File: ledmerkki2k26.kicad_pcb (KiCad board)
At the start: 2 copper layers, 52.2 x 74.7 mm, 71 parts, among them J1 Conn_01x03_Socket, J2 Conn_01x02_Pin, J3 Conn_01x06_Pin, SW1 SW_Push, U1 ATmega328PB-A, Y1 Resonator

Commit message: minor changes to pcb
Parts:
- moved C13 4.75 mm to (101.0, 97.6), turned to 0 degrees
- moved C7 1.28 mm to (90.3, 98.0)
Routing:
- net +5V: track 381.2 -> 379.0 mm
- net DATA: track 21.6 -> 22.6 mm

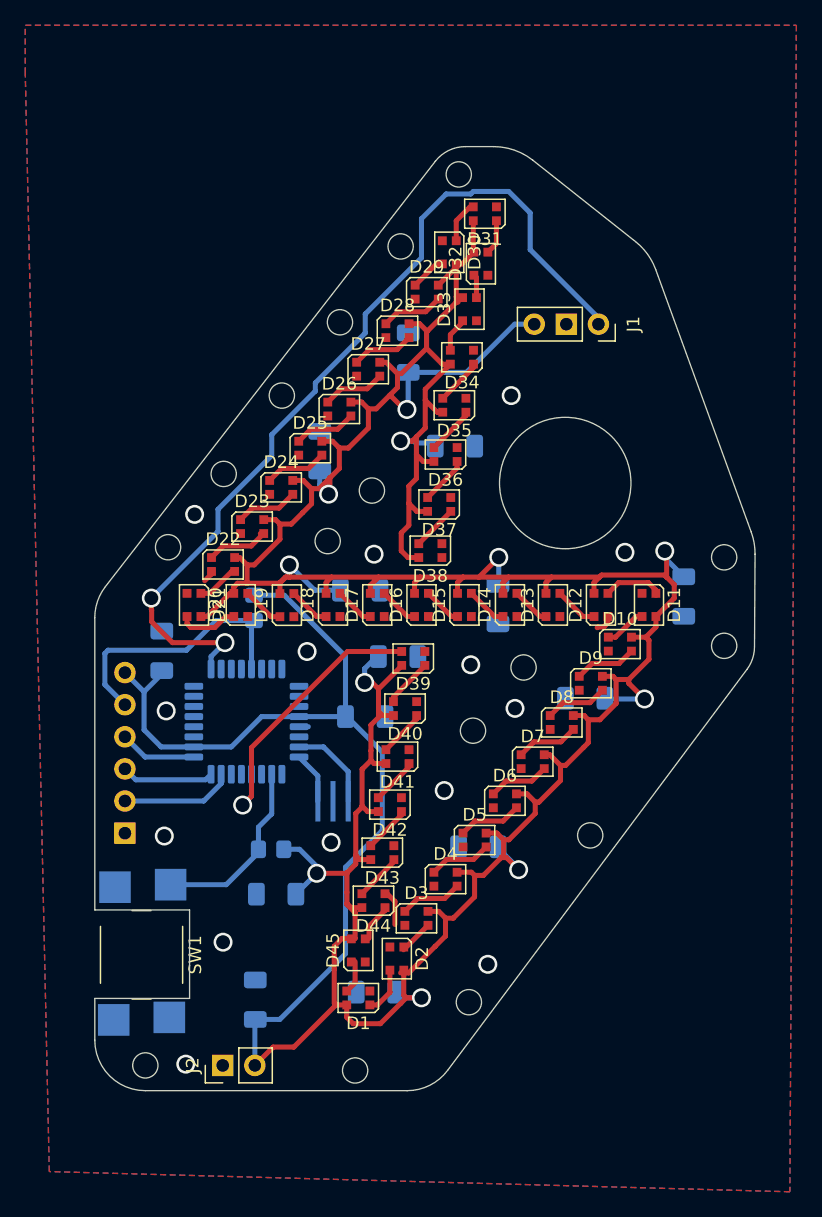
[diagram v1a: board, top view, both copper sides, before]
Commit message: updates to pcb layout and shape, uart pins exposed
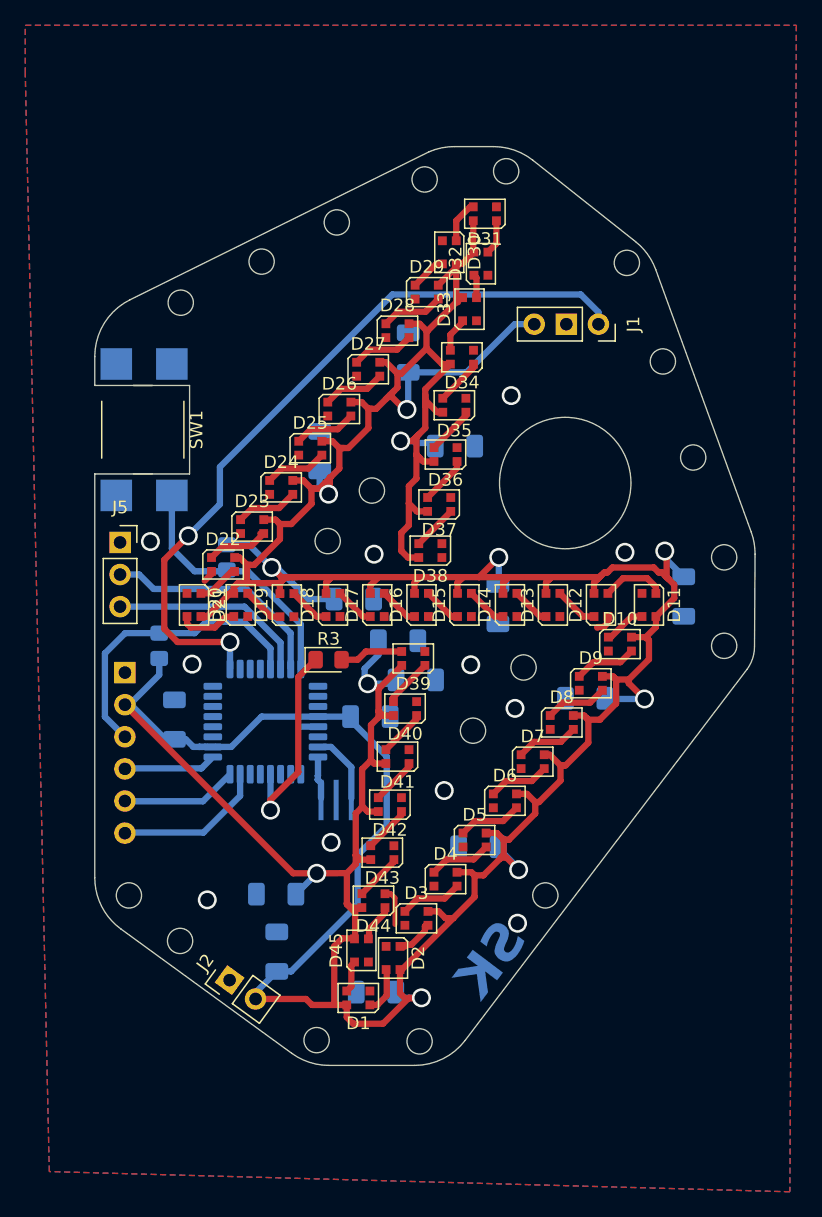
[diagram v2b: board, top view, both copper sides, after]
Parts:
- added C14: 500uF, Capacitor_SMD:C_1206_3216Metric_Pad1.33x1.80mm_HandSolder, B.Cu at (97.9, 116.1)
- added J5: uart, Connector_PinSocket_2.54mm:PinSocket_1x03_P2.54mm_Vertical, F.Cu at (74.5, 105.2)
- added R3: 500R, LED_SMD:LED_0805_2012Metric_Pad1.15x1.40mm_HandSolder, F.Cu at (91.0, 114.5)
- J1: value Conn_01x03_Socket -> mic module header
- J2: value Conn_01x02_Pin -> power header
- J3: value Conn_01x06_Pin -> ISP header
- moved ? 51.7 mm to (78.6, 91.1)
- moved SW1 41.6 mm to (78.6, 93.0)
- moved ? 41.5 mm to (74.2, 101.5)
- moved ? 41.4 mm to (74.2, 91.1)
- moved REF** 30.8 mm to (78.6, 101.5)
- moved R1 23.4 mm to (83.0, 106.4), turned to -90 degrees
- moved R2 8.08 mm to (77.6, 113.4), turned to 90 degrees
- moved J2 6.77 mm to (83.2, 139.8), turned to 54 degrees
- moved C12 5.53 mm to (78.8, 119.2)
- moved C1 4.16 mm to (86.9, 137.6)
- moved U1 1.50 mm to (86.0, 119.4)
- moved C9 1.25 mm to (96.5, 113.0)
- moved C4 0.86 mm to (93.0, 109.7)
- moved C2 0.40 mm to (94.3, 119.0)
- moved D2 0.30 mm to (96.1, 138.1)
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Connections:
- D39 pad 3: DATA -> Net-(D39-DIN)
- J3 pad 1: +5V -> GND
- J3 pad 2: /reset -> +5V
- J3 pad 3: /SCK -> /reset
- J3 pad 4: /MISO -> /SCK
- J3 pad 5: /MOSI -> /MISO
- J3 pad 6: GND -> /MOSI
- U1 pad 10: /button -> unconnected-(U1-PD6-Pad10)
- U1 pad 32: unconnected-(U1-PD2-Pad32) -> /button
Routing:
- net /UART_TX: track 0.00 -> 18.3 mm
- net /UART_RX: track 0.00 -> 16.0 mm
- net /dac: track 71.0 -> 59.6 mm
- net +5V: track 379.0 -> 387.8 mm
- net DATA: track 22.6 -> 16.2 mm
- net /button: track 14.6 -> 20.4 mm
- net Net-(D39-DIN): track 0.00 -> 5.03 mm
- net /MOSI: track 9.77 -> 12.0 mm
- net /MISO: track 7.35 -> 9.18 mm
- net /reset: track 21.5 -> 23.3 mm
- net Net-(U1-XTAL1/PB6): track 7.05 -> 5.31 mm
- net /SCK: track 6.23 -> 7.29 mm
- net Net-(U1-XTAL2/PB7): track 4.12 -> 3.39 mm
- net GND: track 6.06 -> 6.00 mm, vias 14 -> 11
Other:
- board size 52.2 x 74.7 mm -> 52.2 x 72.7 mm
- board text added: "SK"

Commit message: minor fixes
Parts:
- moved C7 1.10 mm to (90.2, 96.9)
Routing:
- net +5V: track 387.8 -> 386.5 mm
- net /MISO: track 9.18 -> 10.1 mm
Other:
- outline, holes or cut-outs redrawn

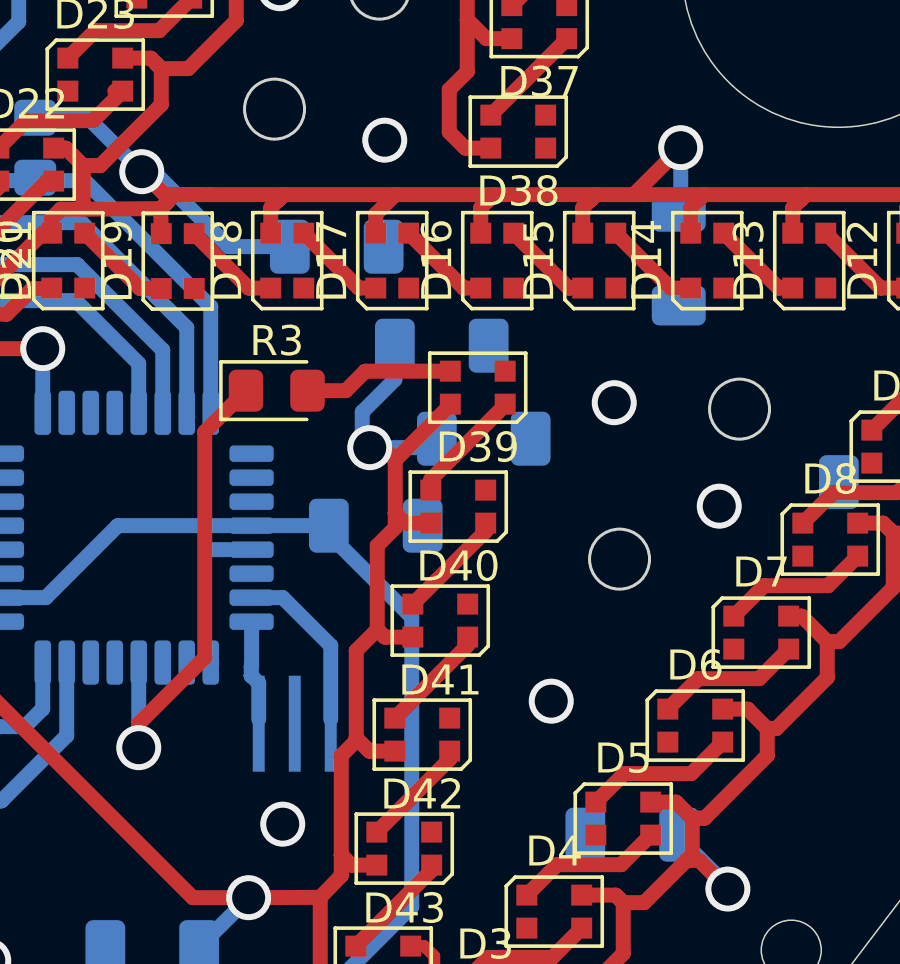
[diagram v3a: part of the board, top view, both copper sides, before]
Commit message: cap footprint added
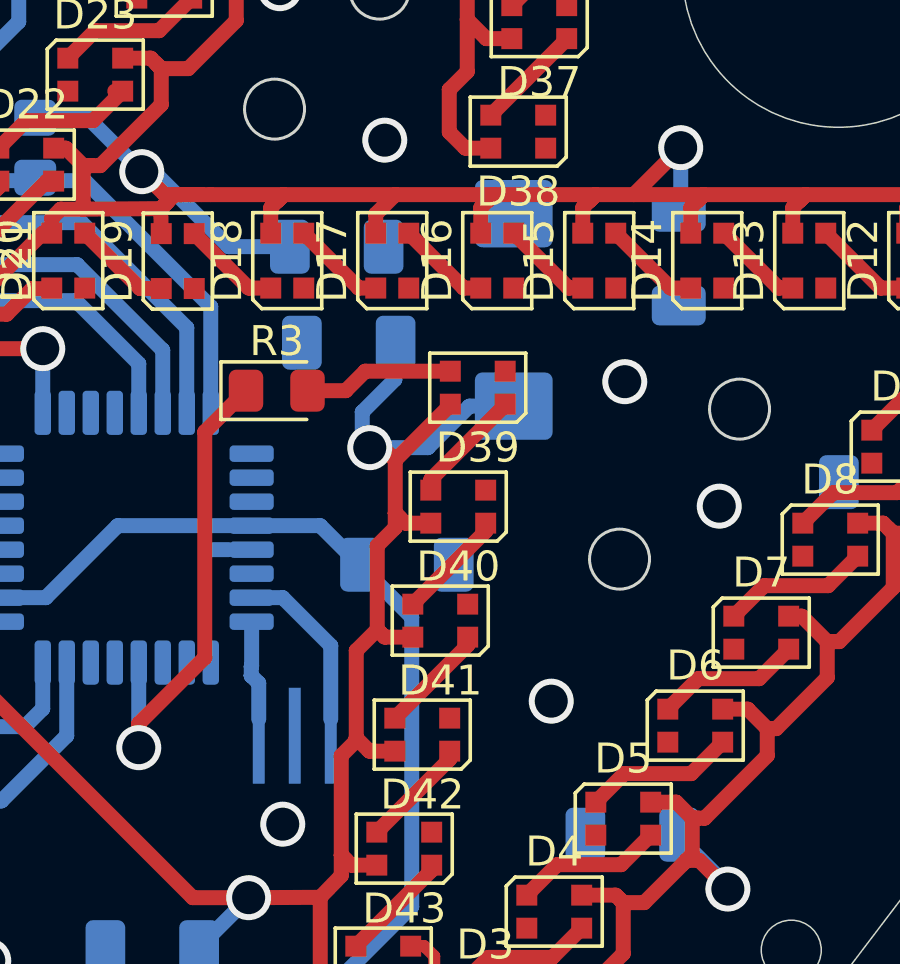
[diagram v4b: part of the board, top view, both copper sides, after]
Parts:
- C14: footprint Capacitor_SMD:C_1206_3216Metric_Pad1.33x1.80mm_HandSolder -> Capacitor_Tantalum_SMD:CP_EIA-7343-15_Kemet-W_HandSolder
- moved C14 4.41 mm to (98.9, 111.8), turned to 90 degrees
- moved C9 3.10 mm to (93.4, 112.9), turned to 180 degrees
- moved C2 1.66 mm to (95.3, 120.3)
- moved Y1 0.40 mm to (91.6, 126.0)
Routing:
- net +5V: track 386.5 -> 389.9 mm
